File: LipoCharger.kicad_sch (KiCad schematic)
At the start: 34 parts, among them J1 S2B-XH-A, J2 USB_C_Receptacle_USB2.0_14P, Q1 SI2300A, Q2 SI2300A, Q3 PMOS, SW1 SK12D07VG4, U1 TP4056-42-ESOP8, U2 MT3608, U3 FM2113

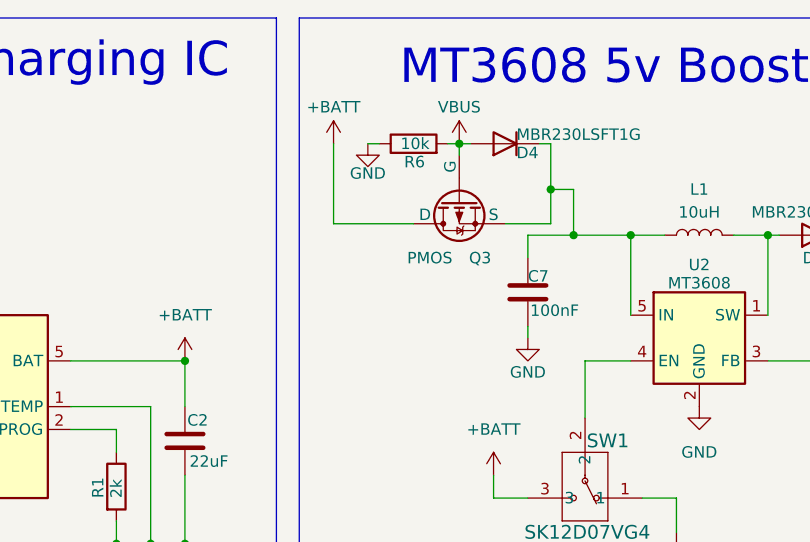
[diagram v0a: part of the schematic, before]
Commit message: added the updated inductor and update the model for the PMOS mosfet (Should update the NMOS)
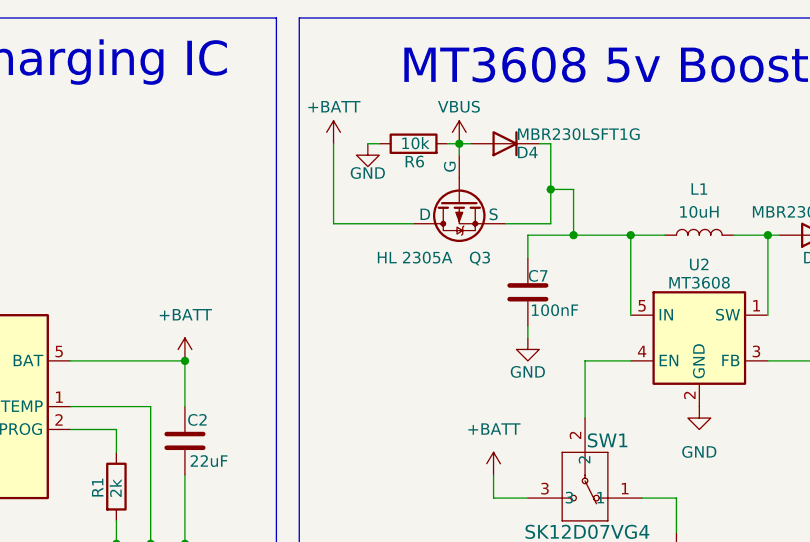
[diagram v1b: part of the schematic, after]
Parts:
- D3: footprint Diode_SMD:D_SMA-SMB_Universal_Handsoldering -> Diode_SMD:D_SOD-123
- D4: footprint (none) -> Diode_SMD:D_SOD-123
- L1: footprint a_Library:WE-PD2_1054 -> a_Library:HY0630-100M-M
- Q3: value PMOS -> HL 2305A; footprint (none) -> Package_TO_SOT_SMD:SOT-23_Handsoldering; LCSC Part # (none) -> C20071223
- R6: footprint (none) -> Resistor_SMD:R_0603_1608Metric_Pad0.98x0.95mm_HandSolder
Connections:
- net +BATT: now also Q3.3 (D); no longer Q3.1 (D)
- net VBUS: now also Q3.1 (G); no longer Q3.2 (G)
- net at C7.1, D4.1 (K), L1.1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: now also Q3.2 (S); no longer Q3.3 (S)
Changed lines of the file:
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@@
 			)
 		)
-		(property "Footprint" "Diode_SMD:D_SMA-SMB_Universal_Handsoldering"
+		(property "Footprint" "Diode_SMD:D_SOD-123"
 			(at 248.92 38.1 0)
 			(effects
@@
 			)
 		)
-		(property "Footprint" ""
+		(property "Footprint" "Diode_SMD:D_SOD-123"
 			(at 214.63 27.94 0)
 			(effects
@@
 			)
 		)
-		(property "Value" "PMOS"
+		(property "Value" "HL 2305A"
 			(at 208.788 40.64 90)
 			(effects
@@
 			)
 		)
-		(property "Footprint" ""
-			(at 207.01 39.37 0)
+		(property "Footprint" "Package_TO_SOT_SMD:SOT-23_Handsoldering"
+			(at 195.834 41.91 0)
 			(effects
 				(font
@@
 		)
 		(property "Description" "P-MOSFET transistor, drain/source/gate"
-			(at 209.55 34.29 0)
+			(at 220.98 35.814 0)
 			(effects
 				(font
@@
 		(property "Sim.Pins" "1=D 2=G 3=S"
 			(at 224.79 34.29 0)
+			(effects
+				(font
+					(size 1.27 1.27)
+				)
+				(hide yes)
+			)
+		)
+		(property "LCSC Part #" "C20071223"
+			(at 200.914 31.496 90)
 			(effects
 				(font
@@
 			)
 		)
-		(property "Footprint" ""
+		(property "Footprint" "Resistor_SMD:R_0603_1608Metric_Pad0.98x0.95mm_HandSolder"
 			(at 204.47 29.718 90)
 			(effects
@@
 			)
 		)
-		(property "Footprint" "a_Library:WE-PD2_1054"
+		(property "Footprint" "a_Library:HY0630-100M-M"
 			(at 236.22 38.1 0)
 			(effects

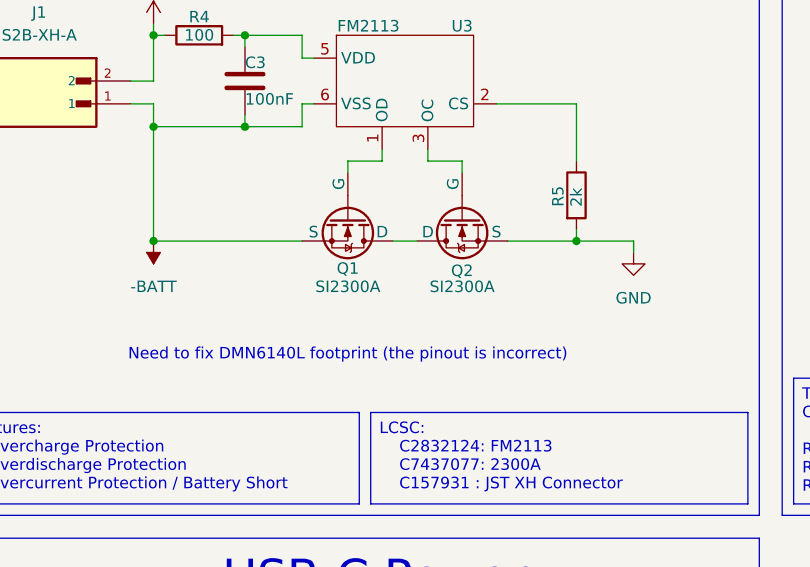
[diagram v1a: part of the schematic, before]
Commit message: fixed nmos footprints
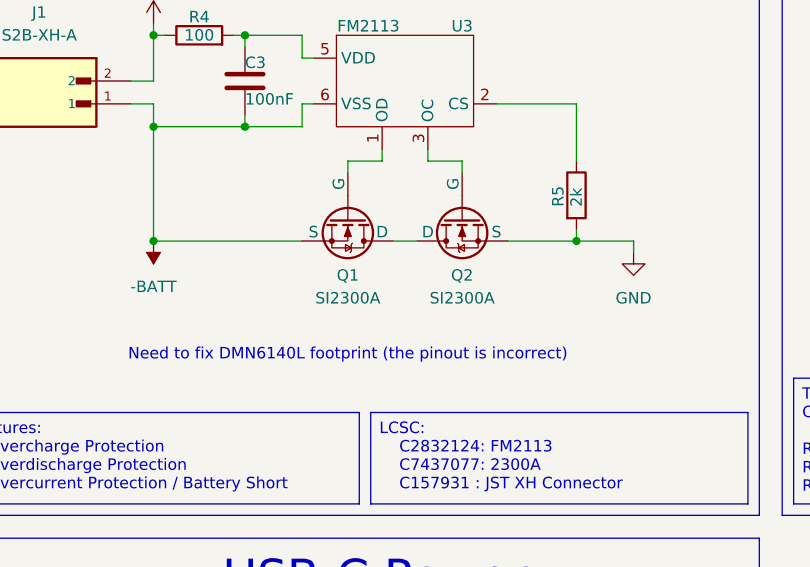
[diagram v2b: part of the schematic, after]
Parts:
- removed Q1, Q2: SI2300A, Package_TO_SOT_SMD:SOT-23_Handsoldering, symbol Simulation_SPICE:NMOS
- added Q1, Q2: SI2300A, Package_TO_SOT_SMD:TSOT-23_HandSoldering, symbol New_Library:SI2300A
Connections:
- net -BATT: now also Q1.2 (S)
- net GND: now also Q2.2 (S)
- net at U3.3 (OC): now also Q2.1 (G)
- net at U3.1 (OD): now also Q1.1 (G)
- new net: Q1.3 (D), Q2.3 (D)
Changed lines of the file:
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@@
-	)
-	(symbol
-		(lib_id "Simulation_SPICE:NMOS")
-		(at 71.12 60.96 90)
-		(mirror x)
-		(unit 1)
-		(exclude_from_sim no)
-		(in_bom yes)
-		(on_board yes)
-		(dnp no)
-		(property "Reference" "Q2"
-			(at 71.12 66.802 90)
-			(effects
-				(font
-					(size 1.27 1.27)
-				)
-			)
-		)
-		(property "Value" "SI2300A"
-			(at 71.12 68.58 90)
-			(effects
-				(font
-					(size 1.27 1.27)
-				)
-			)
-		)
-		(property "Footprint" "Package_TO_SOT_SMD:SOT-23_Handsoldering"
-			(at 68.58 66.04 0)
-			(effects
-				(font
-					(size 1.27 1.27)
-				)
-				(hide yes)
-			)
-		)
-		(property "Datasheet" "https://ngspice.sourceforge.io/docs/ngspice-html-manual/manual.xhtml#cha_MOSFETs"
-			(at 83.82 60.96 0)
-			(effects
-				(font
-					(size 1.27 1.27)
-				)
-				(hide yes)
-			)
-		)
-		(property "Description" "N-MOSFET transistor, drain/source/gate"
-			(at 71.12 60.96 0)
-			(effects
-				(font
-					(size 1.27 1.27)
-				)
-				(hide yes)
-			)
-		)
-		(property "Sim.Device" "NMOS"
-			(at 88.265 60.96 0)
-			(effects
-				(font
-					(size 1.27 1.27)
-				)
-				(hide yes)
-			)
-		)
-		(property "Sim.Type" "VDMOS"
-			(at 90.17 60.96 0)
-			(effects
-				(font
-					(size 1.27 1.27)
-				)
-				(hide yes)
-			)
-		)
-		(property "Sim.Pins" "1=D 2=G 3=S"
-			(at 86.36 60.96 0)
-			(effects
-				(font
-					(size 1.27 1.27)
-				)
-				(hide yes)
-			)
-		)
-		(property "LCSC Part #" "C347480"
-			(at 71.12 60.96 90)
-			(effects
-				(font
-					(size 1.27 1.27)
-				)
-				(hide yes)
-			)
-		)
-		(pin "2"
-		)
-		(pin "1"
-		)
-		(pin "3"
-		)
-		(instances
-			(project "LipoCharger"
-				(path "/b34478b6-339b-4f78-905c-fce6e8fbd016"
-					(reference "Q2")
-					(unit 1)
-				)
-			)
-		)
 	)
 	(symbol
@@
 	)
 	(symbol
+		(lib_id "New_Library:SI2300A")
+		(at 58.42 60.96 270)
+		(unit 1)
+		(exclude_from_sim no)
+		(in_bom yes)
+		(on_board yes)
+		(dnp no)
+		(fields_autoplaced yes)
+		(property "Reference" "Q1"
+			(at 58.42 67.31 90)
+			(effects
+				(font
+					(size 1.27 1.27)
+				)
+			)
+		)
+		(property "Value" "SI2300A"
+			(at 58.42 69.85 90)
+			(effects
+				(font
+					(size 1.27 1.27)
+				)
+			)
+		)
+		(property "Footprint" "Package_TO_SOT_SMD:TSOT-23_HandSoldering"
+			(at 60.96 66.04 0)
+			(effects
+				(font
+					(size 1.27 1.27)
+				)
+				(hide yes)
+			)
+		)
+		(property "Datasheet" "https://ngspice.sourceforge.io/docs/ngspice-html-manual/manual.xhtml#cha_MOSFETs"
+			(at 45.72 60.96 0)
+			(effects
+				(font
+					(size 1.27 1.27)
+				)
+				(hide yes)
+			)
+		)
+		(property "Description" "N-MOSFET transistor, drain/source/gate"
+			(at 58.42 60.96 0)
+			(effects
+				(font
+					(size 1.27 1.27)
+				)
+				(hide yes)
+			)
+		)
+		(property "Sim.Device" "NMOS"
+			(at 41.275 60.96 0)
+			(effects
+				(font
+					(size 1.27 1.27)
+				)
+				(hide yes)
+			)
+		)
+		(property "Sim.Type" "VDMOS"
+			(at 39.37 60.96 0)
+			(effects
+				(font
+					(size 1.27 1.27)
+				)
+				(hide yes)
+			)
+		)
+		(property "Sim.Pins" "1=D 2=G 3=S"
+			(at 43.18 60.96 0)
+			(effects
+				(font
+					(size 1.27 1.27)
+				)
+				(hide yes)
+			)
+		)
+		(pin "1"
+		)
+		(pin "3"
+		)
+		(pin "2"
+		)
+		(instances
+			(project ""
+				(path "/b34478b6-339b-4f78-905c-fce6e8fbd016"
+					(reference "Q1")
+					(unit 1)
+				)
+			)
+		)
+	)
+	(symbol
 		(lib_id "Device:C")
 		(at 46.99 45.72 0)
@@
 	)
 	(symbol
-		(lib_id "Simulation_SPICE:NMOS")
-		(at 58.42 60.96 270)
-		(unit 1)
-		(exclude_from_sim no)
-		(in_bom yes)
-		(on_board yes)
-		(dnp no)
-		(property "Reference" "Q1"
-			(at 58.42 66.548 90)
-			(effects
-				(font
-					(size 1.27 1.27)
-				)
-			)
-		)
-		(property "Value" "SI2300A"
-			(at 58.42 68.58 90)
-			(effects
-				(font
-					(size 1.27 1.27)
-				)
-			)
-		)
-		(property "Footprint" "Package_TO_SOT_SMD:SOT-23_Handsoldering"
-			(at 60.96 66.04 0)
-			(effects
-				(font
-					(size 1.27 1.27)
-				)
-				(hide yes)
-			)
-		)
-		(property "Datasheet" "https://ngspice.sourceforge.io/docs/ngspice-html-manual/manual.xhtml#cha_MOSFETs"
-			(at 45.72 60.96 0)
-			(effects
-				(font
-					(size 1.27 1.27)
-				)
-				(hide yes)
-			)
-		)
-		(property "Description" "N-MOSFET transistor, drain/source/gate"
-			(at 58.42 60.96 0)
-			(effects
-				(font
-					(size 1.27 1.27)
-				)
-				(hide yes)
-			)
-		)
-		(property "Sim.Device" "NMOS"
-			(at 41.275 60.96 0)
-			(effects
-				(font
-					(size 1.27 1.27)
-				)
-				(hide yes)
-			)
-		)
-		(property "Sim.Type" "VDMOS"
-			(at 39.37 60.96 0)
-			(effects
-				(font
-					(size 1.27 1.27)
-				)
-				(hide yes)
-			)
-		)
-		(property "Sim.Pins" "1=D 2=G 3=S"
-			(at 43.18 60.96 0)
-			(effects
-				(font
-					(size 1.27 1.27)
-				)
-				(hide yes)
-			)
-		)
-		(property "LCSC Part #" "C347480"
-			(at 58.42 60.96 90)
-			(effects
-				(font
-					(size 1.27 1.27)
-				)
-				(hide yes)
-			)
-		)
-		(pin "2"
-		)
-		(pin "1"
-		)
-		(pin "3"
-		)
-		(instances
-			(project ""
-				(path "/b34478b6-339b-4f78-905c-fce6e8fbd016"
-					(reference "Q1")
-					(unit 1)
-				)
-			)
-		)
-	)
-	(symbol
 		(lib_id "power:GND")
 		(at 257.81 62.23 0)
@@
 					(unit 1)
 				)
+			)
+		)
+	)
+	(symbol
+		(lib_id "New_Library:SI2300A")
+		(at 71.12 60.96 90)
+		(mirror x)
+		(unit 1)
+		(exclude_from_sim no)
+		(in_bom yes)
+		(on_board yes)
+		(dnp no)
+		(property "Reference" "Q2"
+			(at 71.12 67.31 90)
+			(effects
+				(font
+					(size 1.27 1.27)
+				)
+			)
+		)
+		(property "Value" "SI2300A"
+			(at 71.12 69.85 90)
+			(effects
+				(font
+					(size 1.27 1.27)
+				)
+			)
+		)
+		(property "Footprint" "Package_TO_SOT_SMD:TSOT-23_HandSoldering"
+			(at 68.58 66.04 0)
+			(effects
+				(font
+					(size 1.27 1.27)
+				)
+				(hide yes)
+			)
+		)
+		(property "Datasheet" "https://ngspice.sourceforge.io/docs/ngspice-html-manual/manual.xhtml#cha_MOSFETs"
+			(at 83.82 60.96 0)
+			(effects
+				(font
+					(size 1.27 1.27)
+				)
+				(hide yes)
+			)
+		)
+		(property "Description" "N-MOSFET transistor, drain/source/gate"
+			(at 71.12 60.96 0)
+			(effects
+				(font
+					(size 1.27 1.27)
+				)
+				(hide yes)
+			)
+		)
+		(property "Sim.Device" "NMOS"
+			(at 88.265 60.96 0)
+			(effects
+				(font
+					(size 1.27 1.27)
+				)
+				(hide yes)
+			)
+		)
+		(property "Sim.Type" "VDMOS"
+			(at 90.17 60.96 0)
+			(effects
+				(font
+					(size 1.27 1.27)
+				)
+				(hide yes)
+			)
+		)
+		(property "Sim.Pins" "1=D 2=G 3=S"
+			(at 86.36 60.96 0)
+			(effects
+				(font
+					(size 1.27 1.27)
+				)
+				(hide yes)
+			)
+		)
+		(pin "1"
+		)
+		(pin "3"
+		)
+		(pin "2"
+		)
+		(instances
+			(project ""
+				(path "/b34478b6-339b-4f78-905c-fce6e8fbd016"
+					(reference "Q2")
+					(unit 1)
+				)

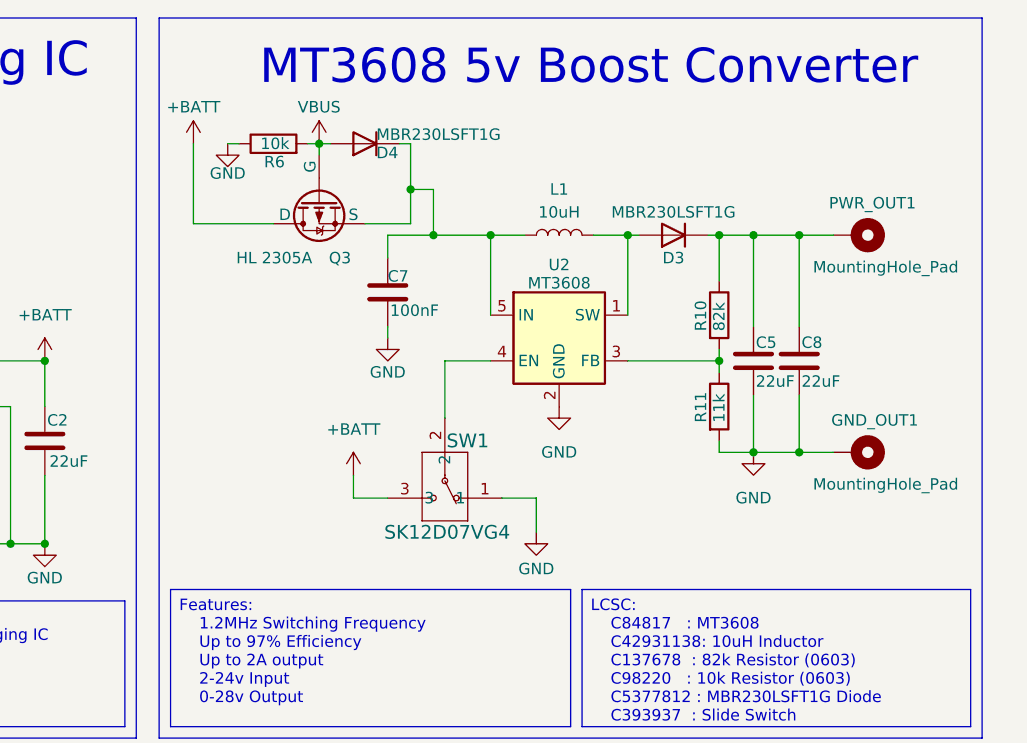
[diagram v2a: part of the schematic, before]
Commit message: Fixed most of the DRC
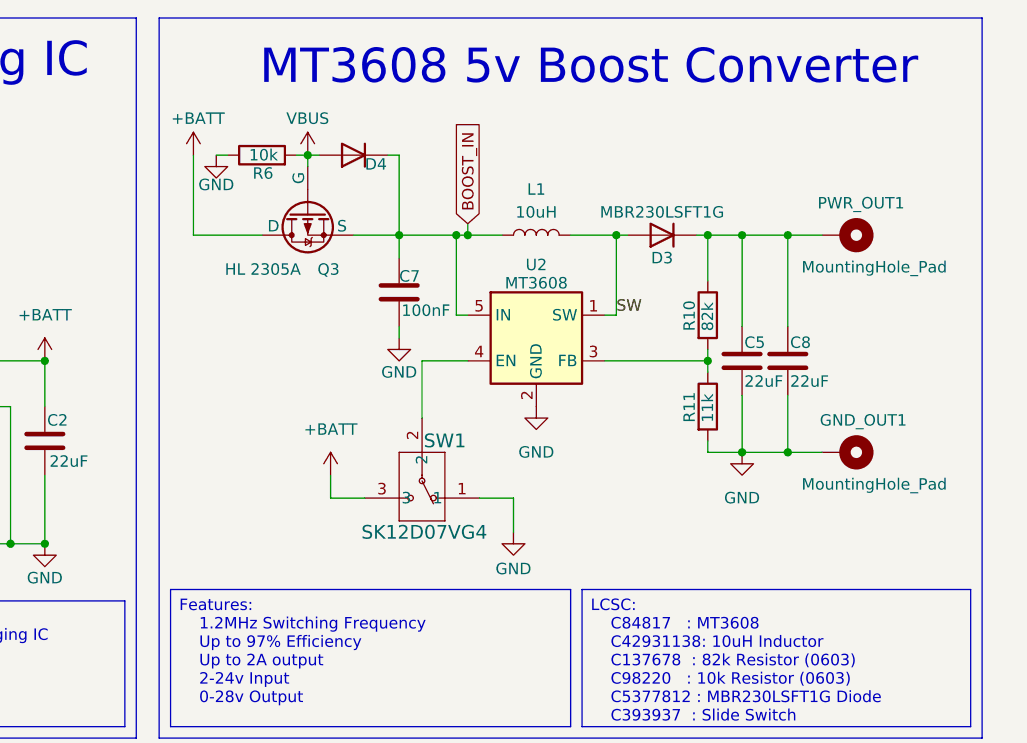
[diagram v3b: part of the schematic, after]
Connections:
- net BOOST_IN: now reaches C7.1, D4.1 (K), L1.1, Q3.2 (S), U2.5 (IN)
- net SW: now reaches D3.2 (A), L1.2, U2.1 (SW)
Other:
- moved on the sheet: C5, C7, C8, D3, D4, GND_OUT1, L1, PWR_OUT1, Q3, R10, R11, R6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

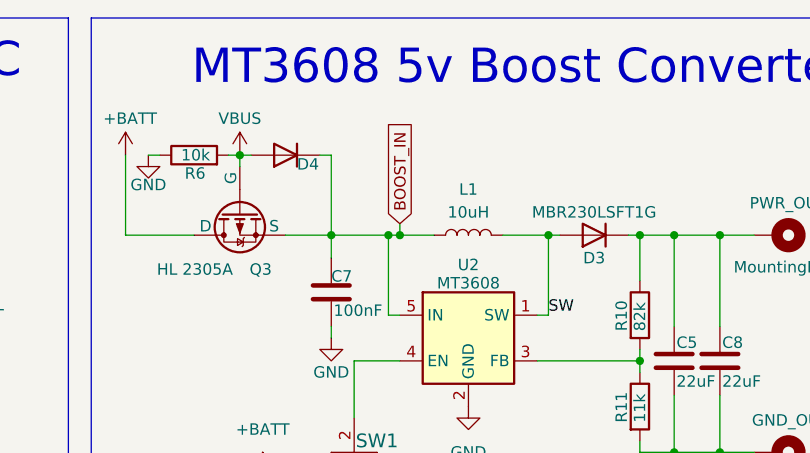
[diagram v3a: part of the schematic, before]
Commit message: Moved vias outside off of the pads
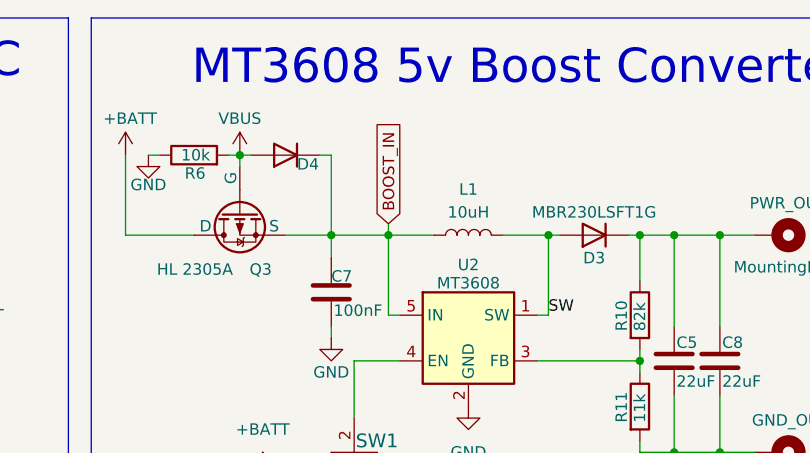
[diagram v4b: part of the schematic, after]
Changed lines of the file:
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@@
-	)
-	(junction
-		(at 226.06 38.1)
-		(diameter 0)
-		(color 0 0 0 0)
 	)
 	(junction
@@
 	(wire
 		(pts
-			(xy 226.06 38.1) (xy 229.87 38.1)
-		)
-		(stroke
-			(width 0)
-			(type default)
-		)
-	)
-	(wire
-		(pts
 			(xy 113.03 38.1) (xy 120.65 38.1)
 		)
@@
 	(wire
 		(pts
-			(xy 226.06 36.83) (xy 226.06 38.1)
+			(xy 224.79 36.83) (xy 224.79 38.1)
 		)
 		(stroke
@@
 	(wire
 		(pts
-			(xy 224.79 38.1) (xy 226.06 38.1)
-		)
-		(stroke
-			(width 0)
-			(type default)
-		)
-	)
-	(wire
-		(pts
 			(xy 175.26 57.15) (xy 175.26 72.39)
 		)
@@
 		(pts
 			(xy 90.17 63.5) (xy 83.82 63.5)
+		)
+		(stroke
+			(width 0)
+			(type default)
+		)
+	)
+	(wire
+		(pts
+			(xy 224.79 38.1) (xy 229.87 38.1)
 		)
 		(stroke
@@
 	(global_label "BOOST_IN"
 		(shape input)
-		(at 226.06 36.83 90)
+		(at 224.79 36.83 90)
 		(fields_autoplaced yes)
 		(effects
@@
 		)
 		(property "Intersheetrefs" "${INTERSHEET_REFS}"
-			(at 226.06 24.8338 90)
+			(at 224.79 24.8338 90)
 			(effects
 				(font

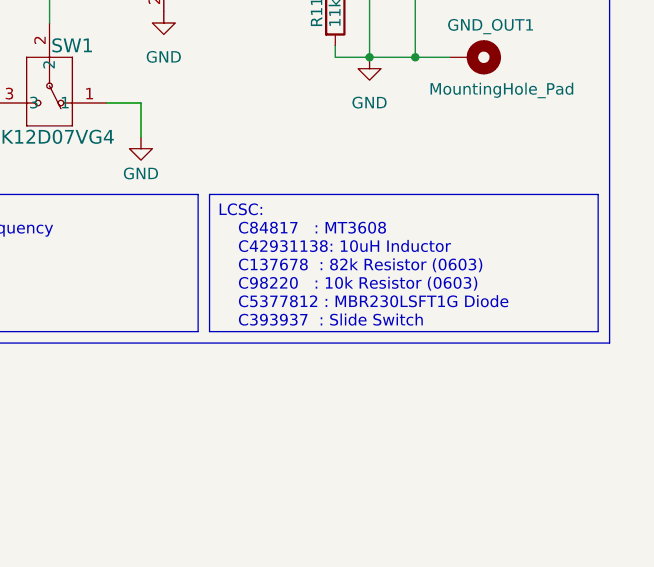
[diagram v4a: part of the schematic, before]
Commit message: Updated LCSC Part Numbers
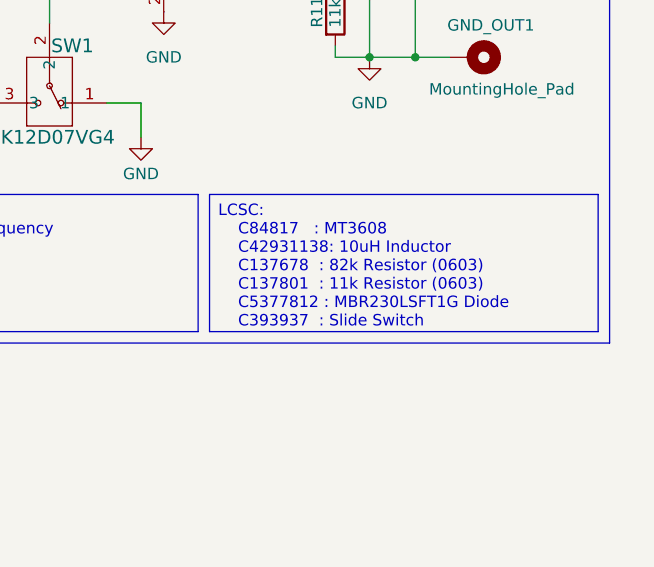
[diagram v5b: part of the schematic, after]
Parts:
- C1, C2: LCSC Part # C19702 -> C6119863
- C3: LCSC Part # C14663 -> C5137636
- C5, C8: LCSC Part # C59461 -> C6119863
- C6: LCSC Part # C19702 -> C5137636
- Q1, Q2: LCSC Part # (none) -> C347480
- R11: LCSC Part # C98220 -> C137801
- R6: LCSC Part # (none) -> C98220
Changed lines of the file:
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@@
 		)
 	)
-	(text_box "LCSC:\n	C84817   : MT3608\n	C42931138: 10uH Inductor\n	C137678  : 82k Resistor (0603)\n	C98220   : 10k Resistor (0603)\n	C5377812 : MBR230LSFT1G Diode\n	C393937  : Slide Switch"
+	(text_box "LCSC:\n	C84817   : MT3608\n	C42931138: 10uH Inductor\n	C137678  : 82k Resistor (0603)\n	C137801  : 11k Resistor (0603)\n	C5377812 : MBR230LSFT1G Diode\n	C393937  : Slide Switch"
 		(exclude_from_sim no)
 		(at 238.76 77.47 0)
@@
 			)
 		)
-		(property "LCSC Part #" "C19702"
+		(property "LCSC Part #" "C5137636"
 			(at 113.03 46.99 0)
 			(effects
@@
 			)
 		)
-		(property "LCSC Part #" "C59461"
+		(property "LCSC Part #" "C6119863"
 			(at 256.54 52.07 0)
 			(effects
@@
 			)
 		)
+		(property "LCSC Part #" "C347480"
+			(at 58.42 60.96 90)
+			(effects
+				(font
+					(size 1.27 1.27)
+				)
+				(hide yes)
+			)
+		)
 		(pin "1"
 		)
@@
 			)
 		)
-		(property "LCSC Part #" "C14663"
+		(property "LCSC Part #" "C5137636"
 			(at 46.99 45.72 0)
 			(effects
@@
 			)
 		)
-		(property "LCSC Part #" "C59461"
+		(property "LCSC Part #" "C6119863"
 			(at 261.62 52.07 0)
 			(effects
@@
 			)
 		)
-		(property "LCSC Part #" "C98220"
+		(property "LCSC Part #" "C137801"
 			(at 252.73 57.15 90)
 			(effects
@@
 			)
 		)
-		(property "LCSC Part #" "C19702"
+		(property "LCSC Part #" "C6119863"
 			(at 179.07 60.96 0)
 			(effects
@@
 			)
 		)
+		(property "LCSC Part #" "C98220"
+			(at 203.2 29.21 90)
+			(effects
+				(font
+					(size 1.27 1.27)
+				)
+				(hide yes)
+			)
+		)
 		(pin "2"
 		)
@@
 			)
 		)
+		(property "LCSC Part #" "C347480"
+			(at 71.12 60.96 90)
+			(effects
+				(font
+					(size 1.27 1.27)
+				)
+				(hide yes)
+			)
+		)
 		(pin "1"
 		)
@@
 			)
 		)
-		(property "LCSC Part #" "C19702"
+		(property "LCSC Part #" "C6119863"
 			(at 120.65 46.99 0)
 			(effects

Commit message: Fixed part number on BOM
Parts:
- C7: LCSC Part # C19702 -> C5137636
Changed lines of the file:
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@@
 			)
 		)
-		(property "LCSC Part #" "C19702"
+		(property "LCSC Part #" "C5137636"
 			(at 218.44 44.45 0)
 			(effects
